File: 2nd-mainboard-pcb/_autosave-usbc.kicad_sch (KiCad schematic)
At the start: 13 parts, among them J1 USB_C_Receptacle, U2 PTS647SM38SMTR2LFS, U5 FT232RL

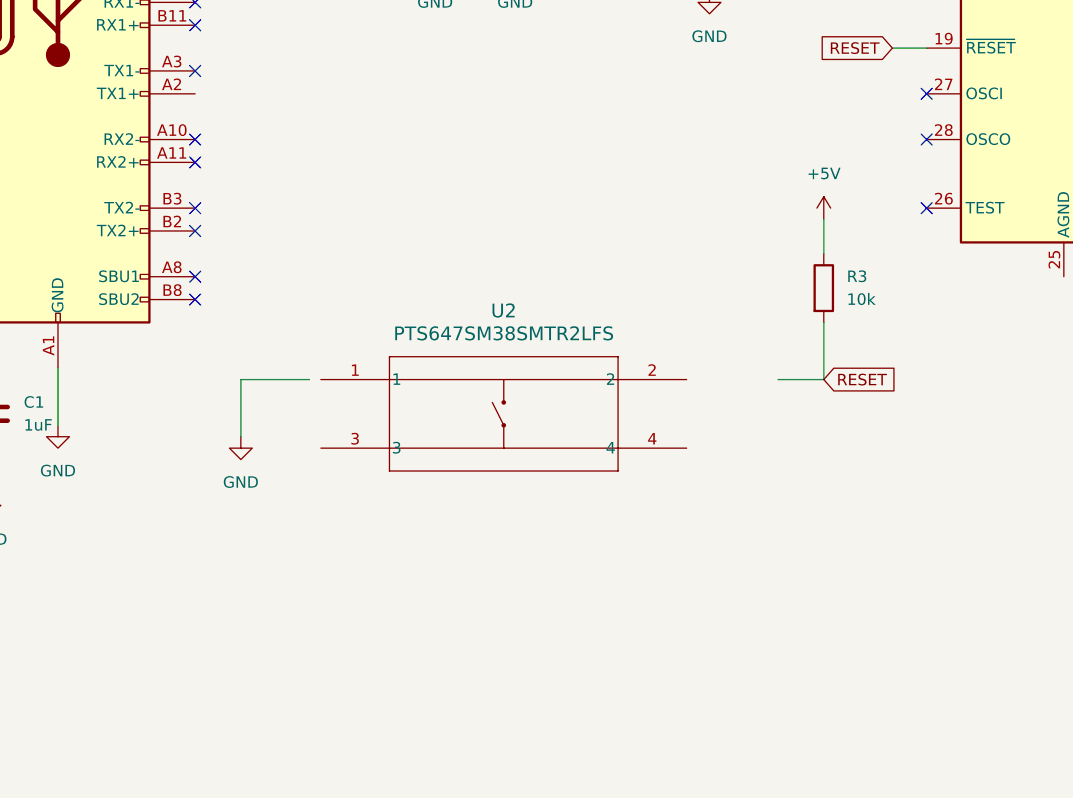
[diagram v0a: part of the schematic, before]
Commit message: aktualisierte Stromverbrauchformeln in excel
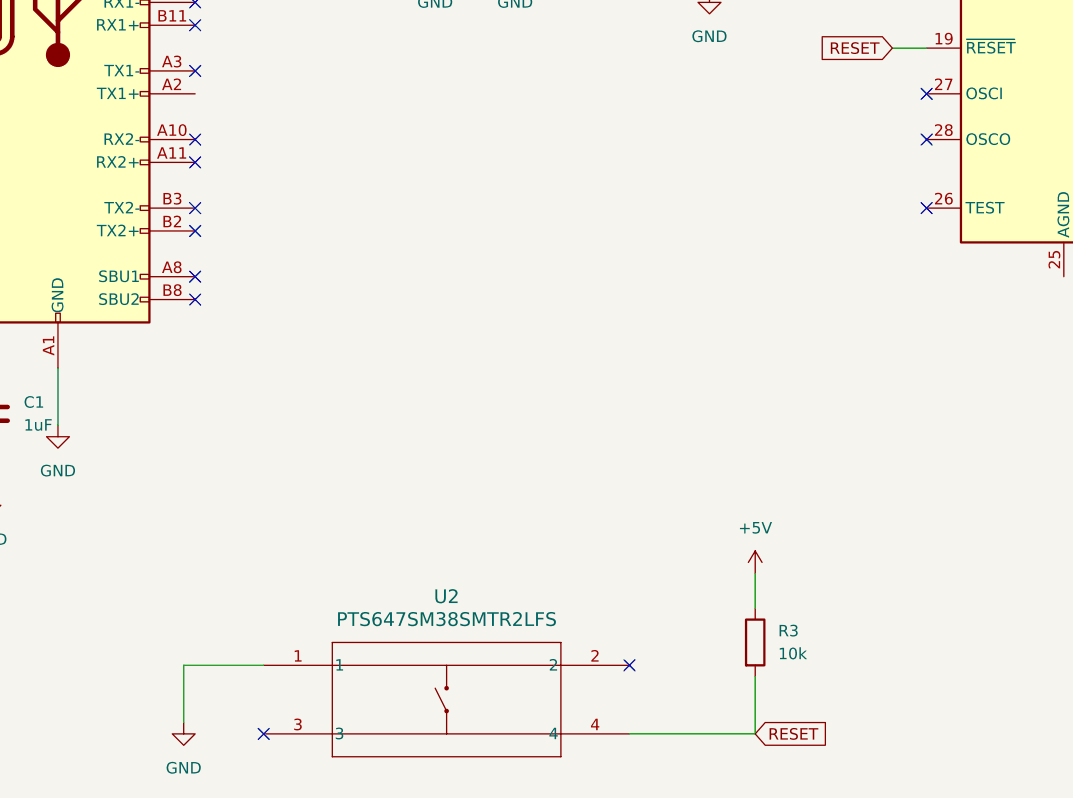
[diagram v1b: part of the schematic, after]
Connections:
- net GND: now also U2.1
- net RESET: now also U2.4
- no-connect marks 21 -> 23
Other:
- moved on the sheet: R3, U2
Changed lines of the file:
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@@
+	)
+	(no_connect
+		(at 64.77 161.29)
 	)
 	(no_connect
@@
 	)
 	(no_connect
+		(at 105.41 153.67)
+	)
+	(no_connect
 		(at 57.15 97.79)
 	)
@@
 	(wire
 		(pts
+			(xy 105.41 161.29) (xy 119.38 161.29)
+		)
+		(stroke
+			(width 0)
+			(type default)
+		)
+	)
+	(wire
+		(pts
 			(xy 114.3 74.93) (xy 114.3 78.74)
 		)
@@
 	(wire
 		(pts
-			(xy 127 104.14) (xy 127 107.95)
+			(xy 119.38 143.51) (xy 119.38 147.32)
 		)
 		(stroke
@@
 	(wire
 		(pts
-			(xy 62.23 121.92) (xy 62.23 128.27)
+			(xy 55.88 153.67) (xy 55.88 160.02)
 		)
 		(stroke
@@
 	(wire
 		(pts
-			(xy 121.92 121.92) (xy 127 121.92)
-		)
-		(stroke
-			(width 0)
-			(type default)
-		)
-	)
-	(wire
-		(pts
 			(xy 114.3 67.31) (xy 127 67.31)
 		)
@@
 	(wire
 		(pts
-			(xy 69.85 121.92) (xy 62.23 121.92)
-		)
-		(stroke
-			(width 0)
-			(type default)
-		)
-	)
-	(wire
-		(pts
-			(xy 127 121.92) (xy 127 115.57)
+			(xy 55.88 153.67) (xy 64.77 153.67)
+		)
+		(stroke
+			(width 0)
+			(type default)
+		)
+	)
+	(wire
+		(pts
+			(xy 119.38 161.29) (xy 119.38 154.94)
 		)
 		(stroke
@@
 	(global_label "RESET"
 		(shape input)
-		(at 127 121.92 0)
+		(at 119.38 161.29 0)
 		(fields_autoplaced yes)
 		(effects
@@
 		)
 		(property "Intersheetrefs" "${INTERSHEET_REFS}"
-			(at 135.7303 121.92 0)
+			(at 128.1103 161.29 0)
 			(effects
 				(font
@@
 	(symbol
 		(lib_id "power:GND")
-		(at 62.23 128.27 0)
+		(at 55.88 160.02 0)
 		(unit 1)
 		(exclude_from_sim no)
@@
 		(fields_autoplaced yes)
 		(property "Reference" "#PWR03"
-			(at 62.23 134.62 0)
+			(at 55.88 166.37 0)
 			(effects
 				(font
@@
 		)
 		(property "Value" "GND"
-			(at 62.23 133.35 0)
+			(at 55.88 165.1 0)
 			(effects
 				(font
@@
 		)
 		(property "Footprint" ""
-			(at 62.23 128.27 0)
+			(at 55.88 160.02 0)
 			(effects
 				(font
@@
 		)
 		(property "Datasheet" ""
-			(at 62.23 128.27 0)
+			(at 55.88 160.02 0)
 			(effects
 				(font
@@
 		)
 		(property "Description" "Power symbol creates a global label with name \"GND\" , ground"
-			(at 62.23 128.27 0)
+			(at 55.88 160.02 0)
 			(effects
 				(font
@@
 	(symbol
 		(lib_id "Device:R")
-		(at 127 111.76 0)
+		(at 119.38 151.13 0)
 		(unit 1)
 		(exclude_from_sim no)
@@
 		(fields_autoplaced yes)
 		(property "Reference" "R3"
-			(at 129.54 110.4899 0)
+			(at 121.92 149.8599 0)
 			(effects
 				(font
@@
 		)
 		(property "Value" "10k"
-			(at 129.54 113.0299 0)
+			(at 121.92 152.3999 0)
 			(effects
 				(font
@@
 		)
 		(property "Footprint" ""
-			(at 125.222 111.76 90)
+			(at 117.602 151.13 90)
 			(effects
 				(font
@@
 		)
 		(property "Datasheet" "~"
-			(at 127 111.76 0)
+			(at 119.38 151.13 0)
 			(effects
 				(font
@@
 		)
 		(property "Description" "Resistor"
-			(at 127 111.76 0)
+			(at 119.38 151.13 0)
 			(effects
 				(font
@@
 	(symbol
 		(lib_id "Imported_Component_Symbols:PTS647SM38SMTR2LFS")
-		(at 71.12 121.92 0)
+		(at 64.77 153.67 0)
 		(unit 1)
 		(exclude_from_sim no)
@@
 		(fields_autoplaced yes)
 		(property "Reference" "U2"
-			(at 91.44 114.3 0)
+			(at 85.09 146.05 0)
 			(effects
 				(font
@@
 		)
 		(property "Value" "PTS647SM38SMTR2LFS"
-			(at 91.44 116.84 0)
+			(at 85.09 148.59 0)
 			(effects
 				(font
@@
 		)
 		(property "Footprint" "SW_PTS647SM38SMTR2LFS_CNK"
-			(at 67.31 114.808 0)
+			(at 60.96 146.558 0)
 			(effects
 				(font
@@
 		)
 		(property "Datasheet" "PTS647SM38SMTR2LFS"
-			(at 66.04 117.602 0)
+			(at 59.69 149.352 0)
 			(effects
 				(font
@@
 		)
 		(property "Description" ""
-			(at 71.12 121.92 0)
+			(at 64.77 153.67 0)
 			(effects
 				(font
@@
 	(symbol
 		(lib_id "power:+5V")
-		(at 127 104.14 0)
+		(at 119.38 143.51 0)
 		(unit 1)
 		(exclude_from_sim no)
@@
 		(fields_autoplaced yes)
 		(property "Reference" "#PWR014"
-			(at 127 107.95 0)
+			(at 119.38 147.32 0)
 			(effects
 				(font
@@
 		)
 		(property "Value" "+5V"
-			(at 127 99.06 0)
+			(at 119.38 138.43 0)
 			(effects
 				(font
@@
 		)
 		(property "Footprint" ""
-			(at 127 104.14 0)
+			(at 119.38 143.51 0)
 			(effects
 				(font
@@
 		)
 		(property "Datasheet" ""
-			(at 127 104.14 0)
+			(at 119.38 143.51 0)
 			(effects
 				(font
@@
 		)
 		(property "Description" "Power symbol creates a global label with name \"+5V\""
-			(at 127 104.14 0)
-			(effects
-				(font
+			(at 119.38 143.51 0)
+			(effects
+				(font
